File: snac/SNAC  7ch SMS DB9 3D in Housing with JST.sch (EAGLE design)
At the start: 42 parts, among them IC1 4030D, IC2 MAX660CPACS, Q1 BSS138, Q2 BSS138, Q3 BSS138, Q4 BSS138, Q5 BSS138, Q6 BSS138, Q7 BSS138, Q9 BC849SMD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

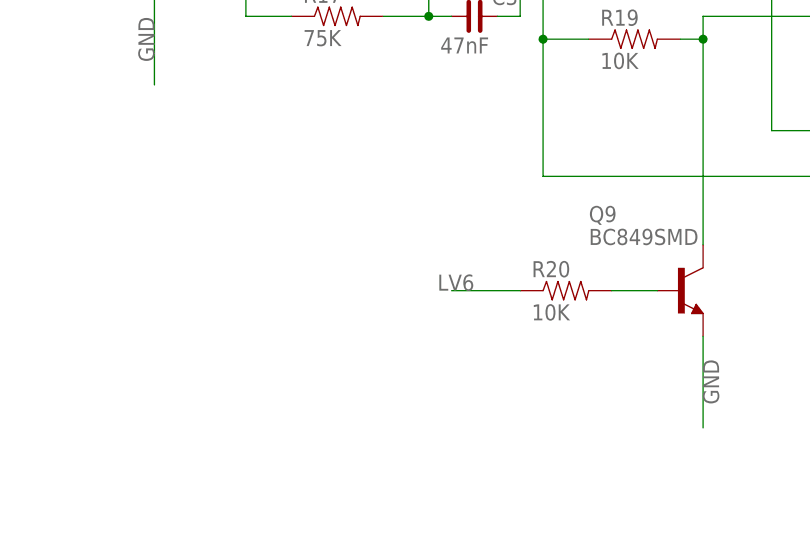
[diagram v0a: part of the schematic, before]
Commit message: LV6/LV7 selection jumper added to SMS 3D board
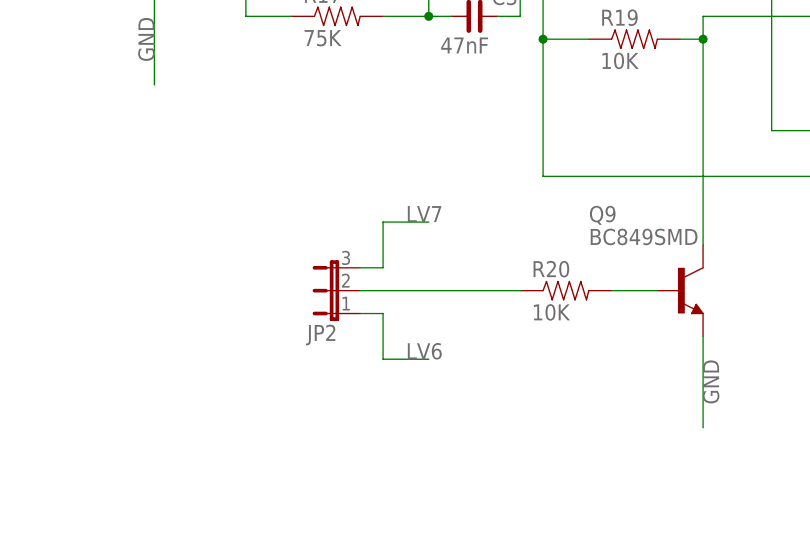
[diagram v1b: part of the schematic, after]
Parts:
- added JP2: (no value), jumper:JP2E
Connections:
- new net N$27: JP2.2, R20.1
- net LV6: now also JP2.1; no longer R20.1
- net LV7: now also JP2.3

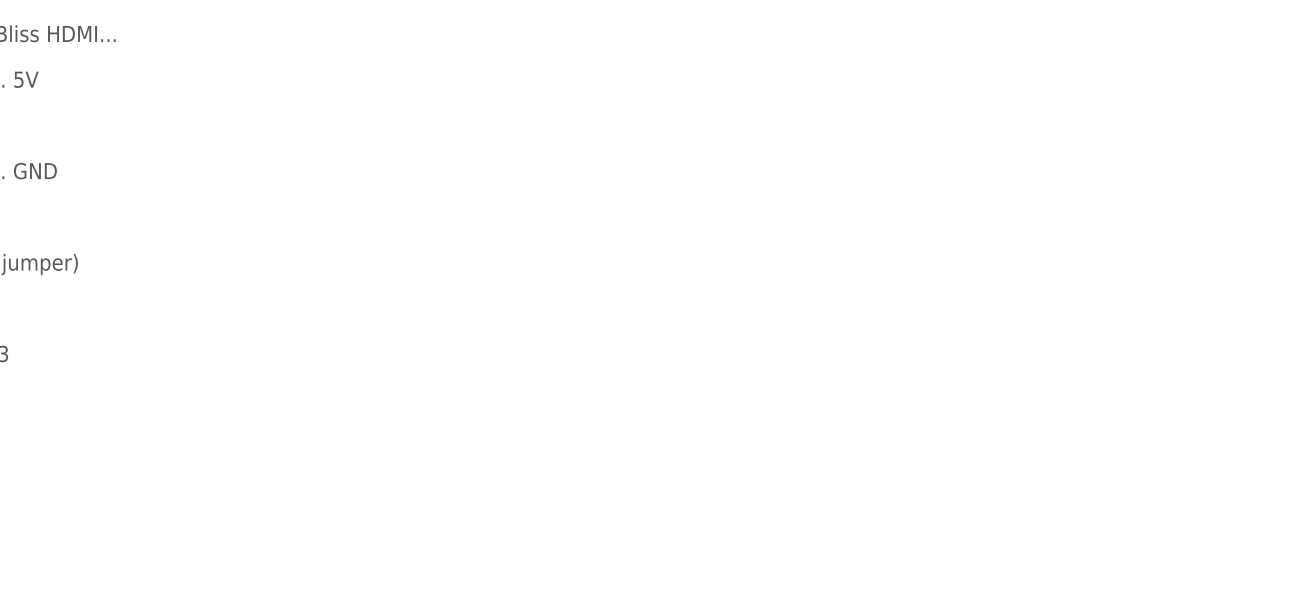
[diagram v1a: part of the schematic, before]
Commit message: Added note to SMS 3D board about USB 3.0 wire colour swaps
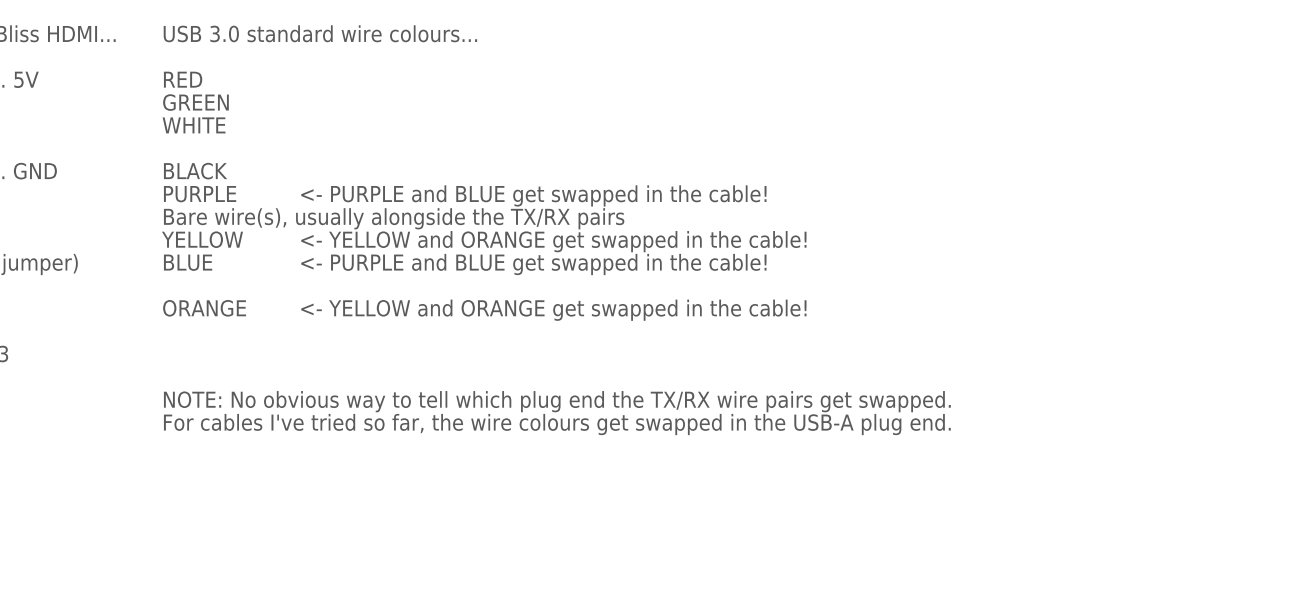
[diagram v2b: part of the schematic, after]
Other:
- note added: "<- PURPLE and BLUE get swapped in the cable!"
- note added: "<- YELLOW and ORANGE get swapped in the cable!"
- note added: "Bare wire(s), usually alongside the TX/RX pairs"
- note added: "For cables I've tried so far, the wire colours get swapped in the USB-A plug end."
- note added: "NOTE: No obvious way to tell which plug end the TX/RX wire pairs get swapped."
- note added: "USB 3.0 standard wire colours..."
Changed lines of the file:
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@@
 <text x="30.48" y="86.36" size="1.778" layer="97">Note: Pin mapping FIXED,
 vs the first prototype!</text>
+<text x="467.36" y="251.46" size="1.778" layer="97">USB 3.0 standard wire colours...</text>
+<text x="467.36" y="246.38" size="1.778" layer="97">RED</text>
+<text x="467.36" y="241.3" size="1.778" layer="97">WHITE</text>
+<text x="467.36" y="243.84" size="1.778" layer="97">GREEN</text>
+<text x="467.36" y="236.22" size="1.778" layer="97">BLACK</text>
+<text x="467.36" y="233.68" size="1.778" layer="97">PURPLE</text>
+<text x="467.36" y="231.14" size="1.778" layer="97">Bare wire(s), usually alongside the TX/RX pairs</text>
+<text x="467.36" y="228.6" size="1.778" layer="97">YELLOW</text>
+<text x="467.36" y="226.06" size="1.778" layer="97">BLUE</text>
+<text x="467.36" y="220.98" size="1.778" layer="97">ORANGE</text>
+<text x="482.6" y="233.68" size="1.778" layer="97">&lt;- PURPLE and BLUE get swapped in the cable!</text>
+<text x="482.6" y="226.06" size="1.778" layer="97">&lt;- PURPLE and BLUE get swapped in the cable!</text>
+<text x="482.6" y="228.6" size="1.778" layer="97">&lt;- YELLOW and ORANGE get swapped in the cable!</text>
+<text x="482.6" y="220.98" size="1.778" layer="97">&lt;- YELLOW and ORANGE get swapped in the cable!</text>
+<text x="467.36" y="210.82" size="1.778" layer="97">NOTE: No obvious way to tell which plug end the TX/RX wire pairs get swapped.</text>
+<text x="467.36" y="208.28" size="1.778" layer="97">For cables I've tried so far, the wire colours get swapped in the USB-A plug end.</text>
 </plain>
 <instances>
